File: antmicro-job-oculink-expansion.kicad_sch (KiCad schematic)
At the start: 105 parts, among them J1 OCuLink_x4_Amphenol_G14A42121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, J2 Plug_Samtec_ERM8_2x40_ERM8-04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, U1 MAX3373EEKA+, U2 PI3EQX16904GL, U3 PI3EQX16904GL

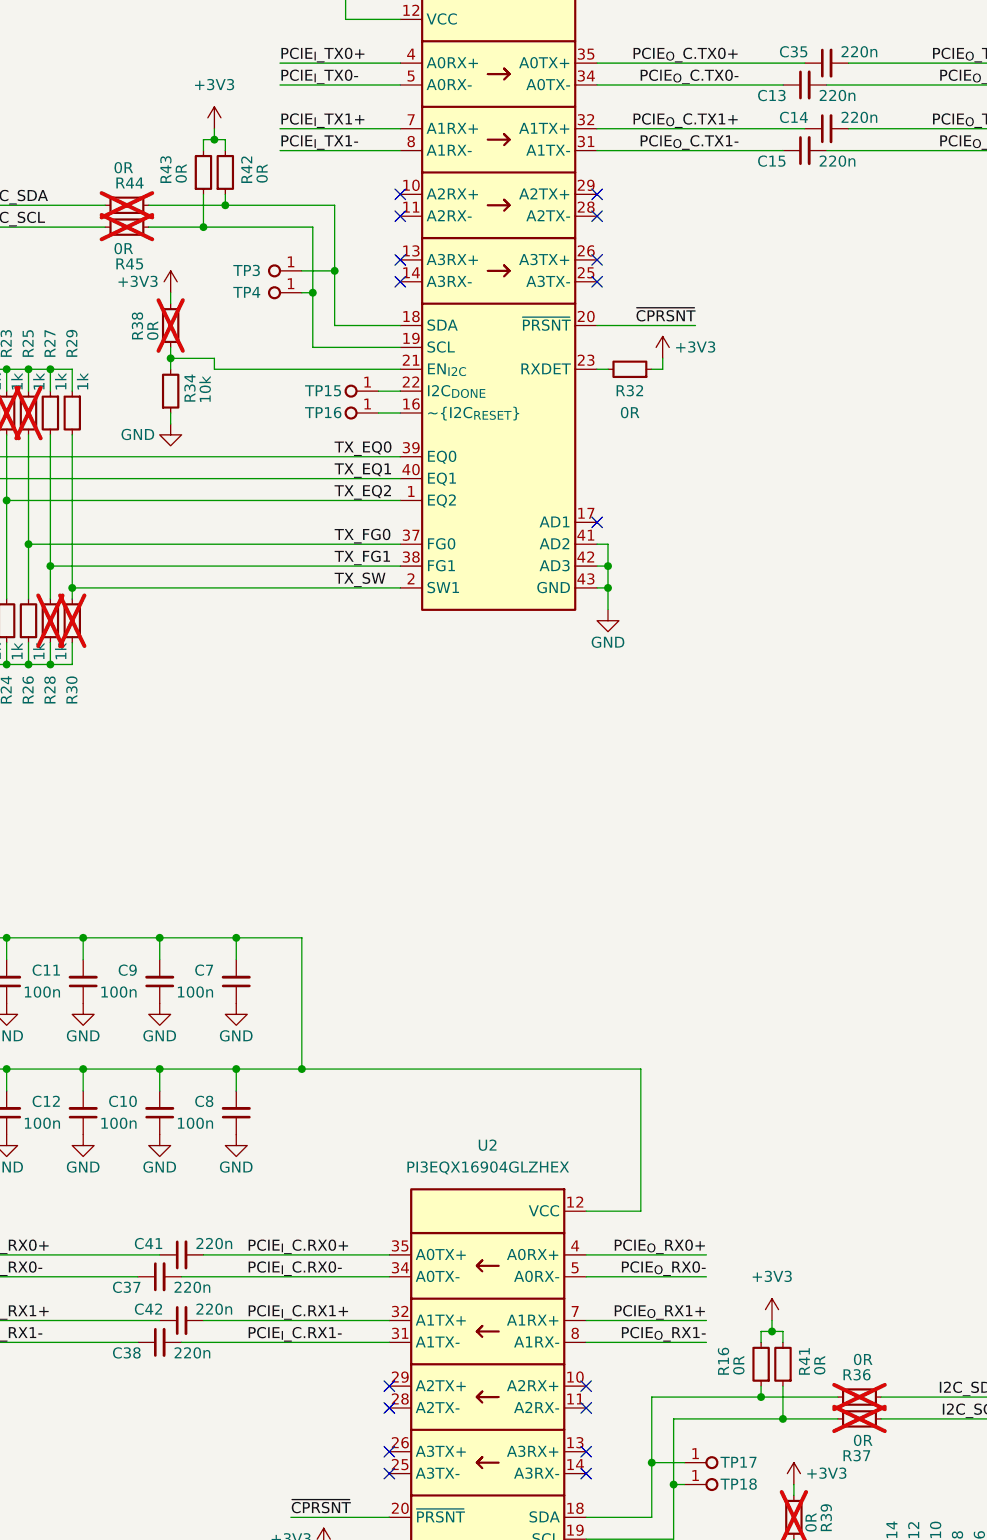
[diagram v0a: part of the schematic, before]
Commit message: [#76297] Fix I2C pull-up resistor value
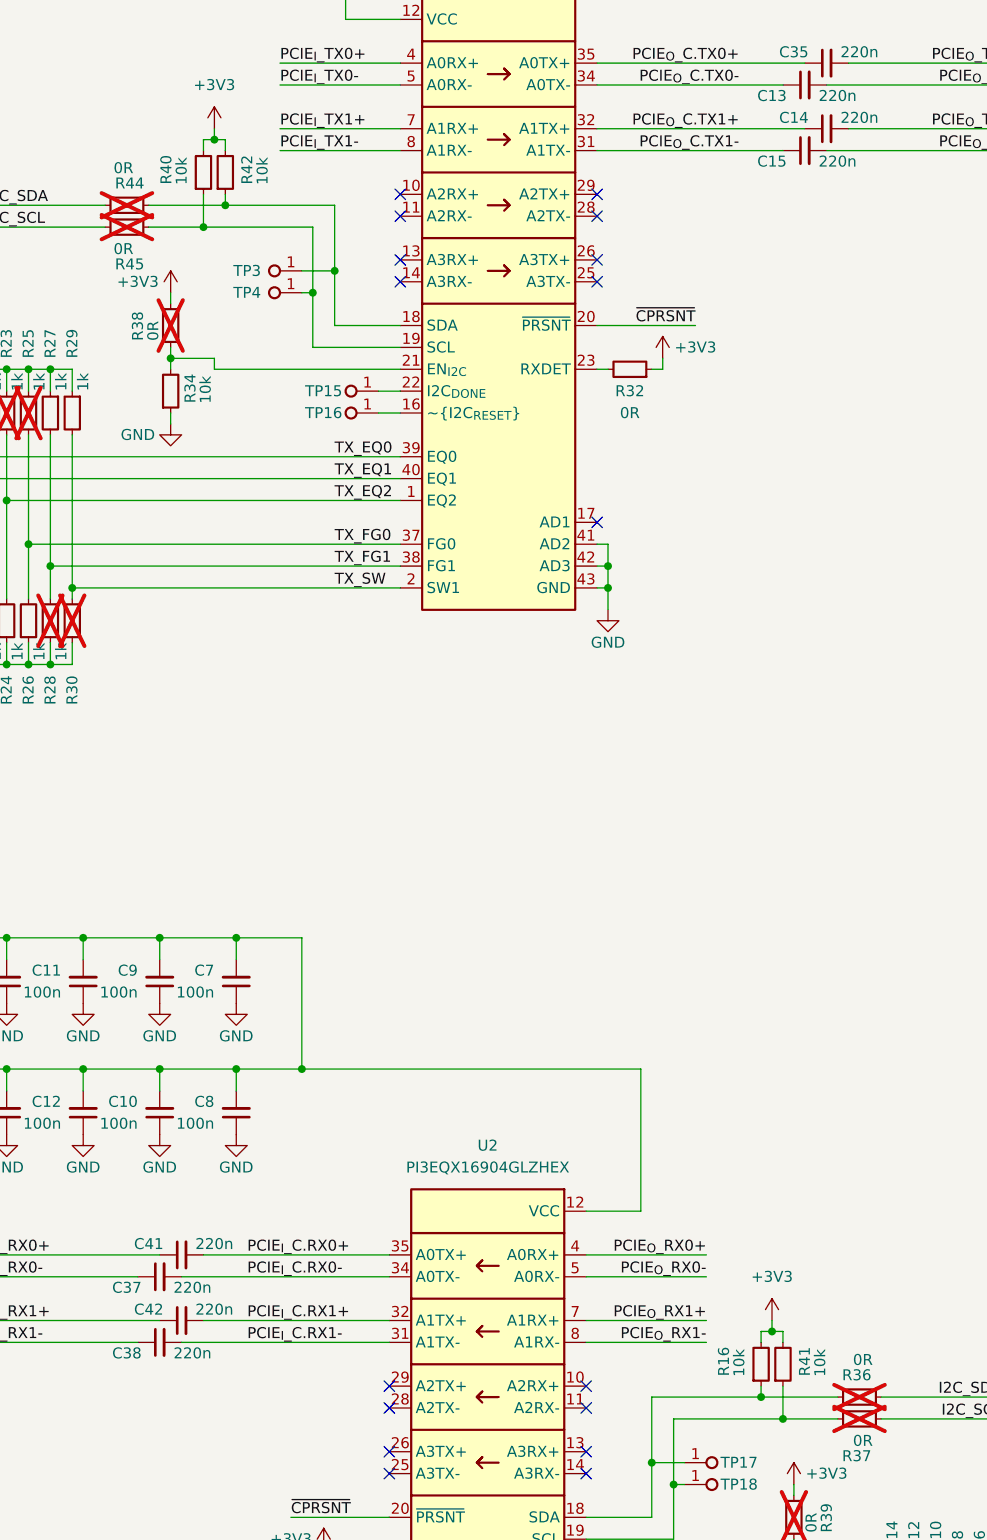
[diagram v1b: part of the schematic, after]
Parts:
- removed R16, R41, R42, R43: R_0R_0402, antmicro-footprints:R_0402_1005Metric, symbol antmicroResistors0402:R_0R_0402
- added R16, R40, R41, R42: R_10k_0402, antmicro-footprints:R_0402_1005Metric, symbol antmicroResistors0402:R_10k_0402
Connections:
- net +3V3: now also R16.2, R40.2, R41.2, R42.2
- net at R36.2, TP17.1, U2.18 (SDA): now also R16.1
- net at R44.2, TP3.1, U3.18 (SDA): now also R42.1
- net at R45.2, TP4.1, U3.19 (SCL): now also R40.1
- net at R37.2, TP18.1, U2.19 (SCL): now also R41.1

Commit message: [#76297] Fix Antmicro logo footprint not matching schematic
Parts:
- N2, N4: footprint antmicro-footprints:antmicro-logo -> antmicro-footprints:antmicro-logo_scaled_15mm
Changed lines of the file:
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@@
 			)
 		)
-		(property "Footprint" "antmicro-footprints:antmicro-logo"
+		(property "Footprint" "antmicro-footprints:antmicro-logo_scaled_15mm"
 			(at 60.96 273.05 0)
 			(effects
@@
 			)
 		)
-		(property "Footprint" "antmicro-footprints:antmicro-logo"
+		(property "Footprint" "antmicro-footprints:antmicro-logo_scaled_15mm"
 			(at 60.96 280.67 0)
 			(effects

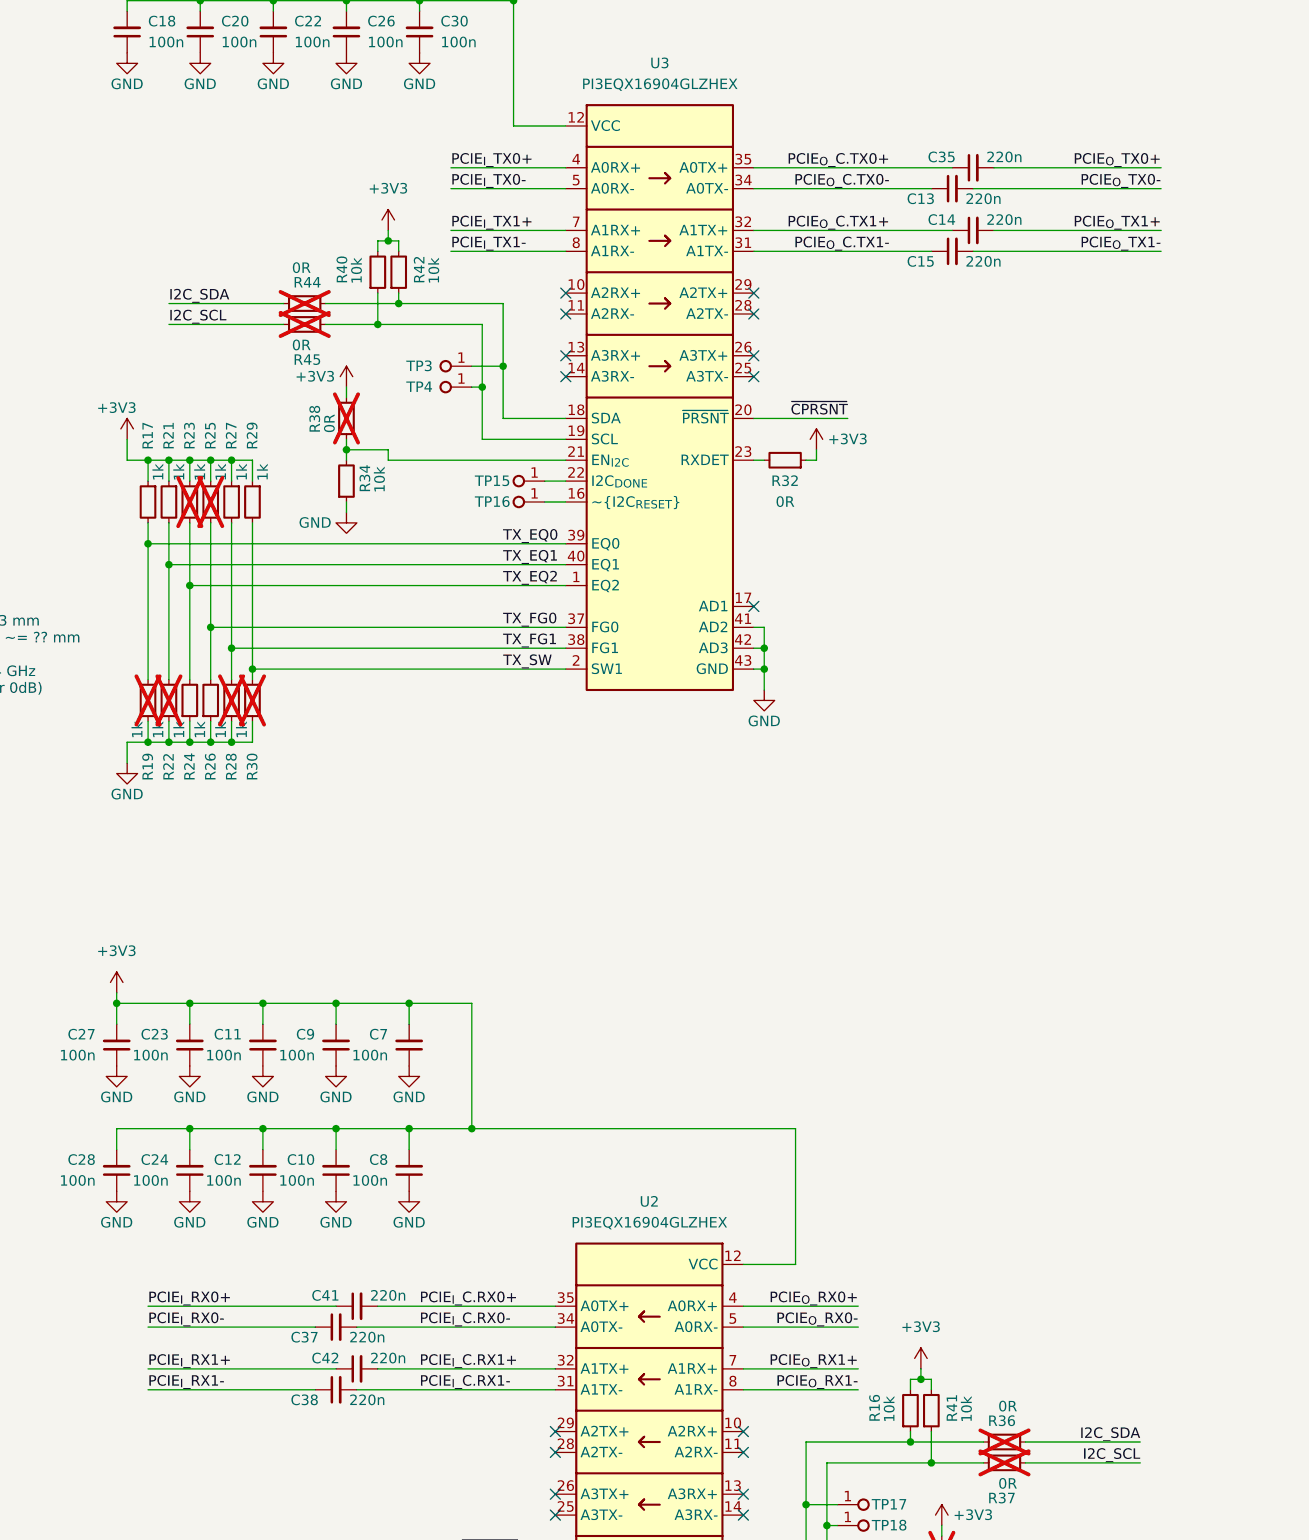
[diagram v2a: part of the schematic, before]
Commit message: [#76297] Reorder redriver PCIe lanes
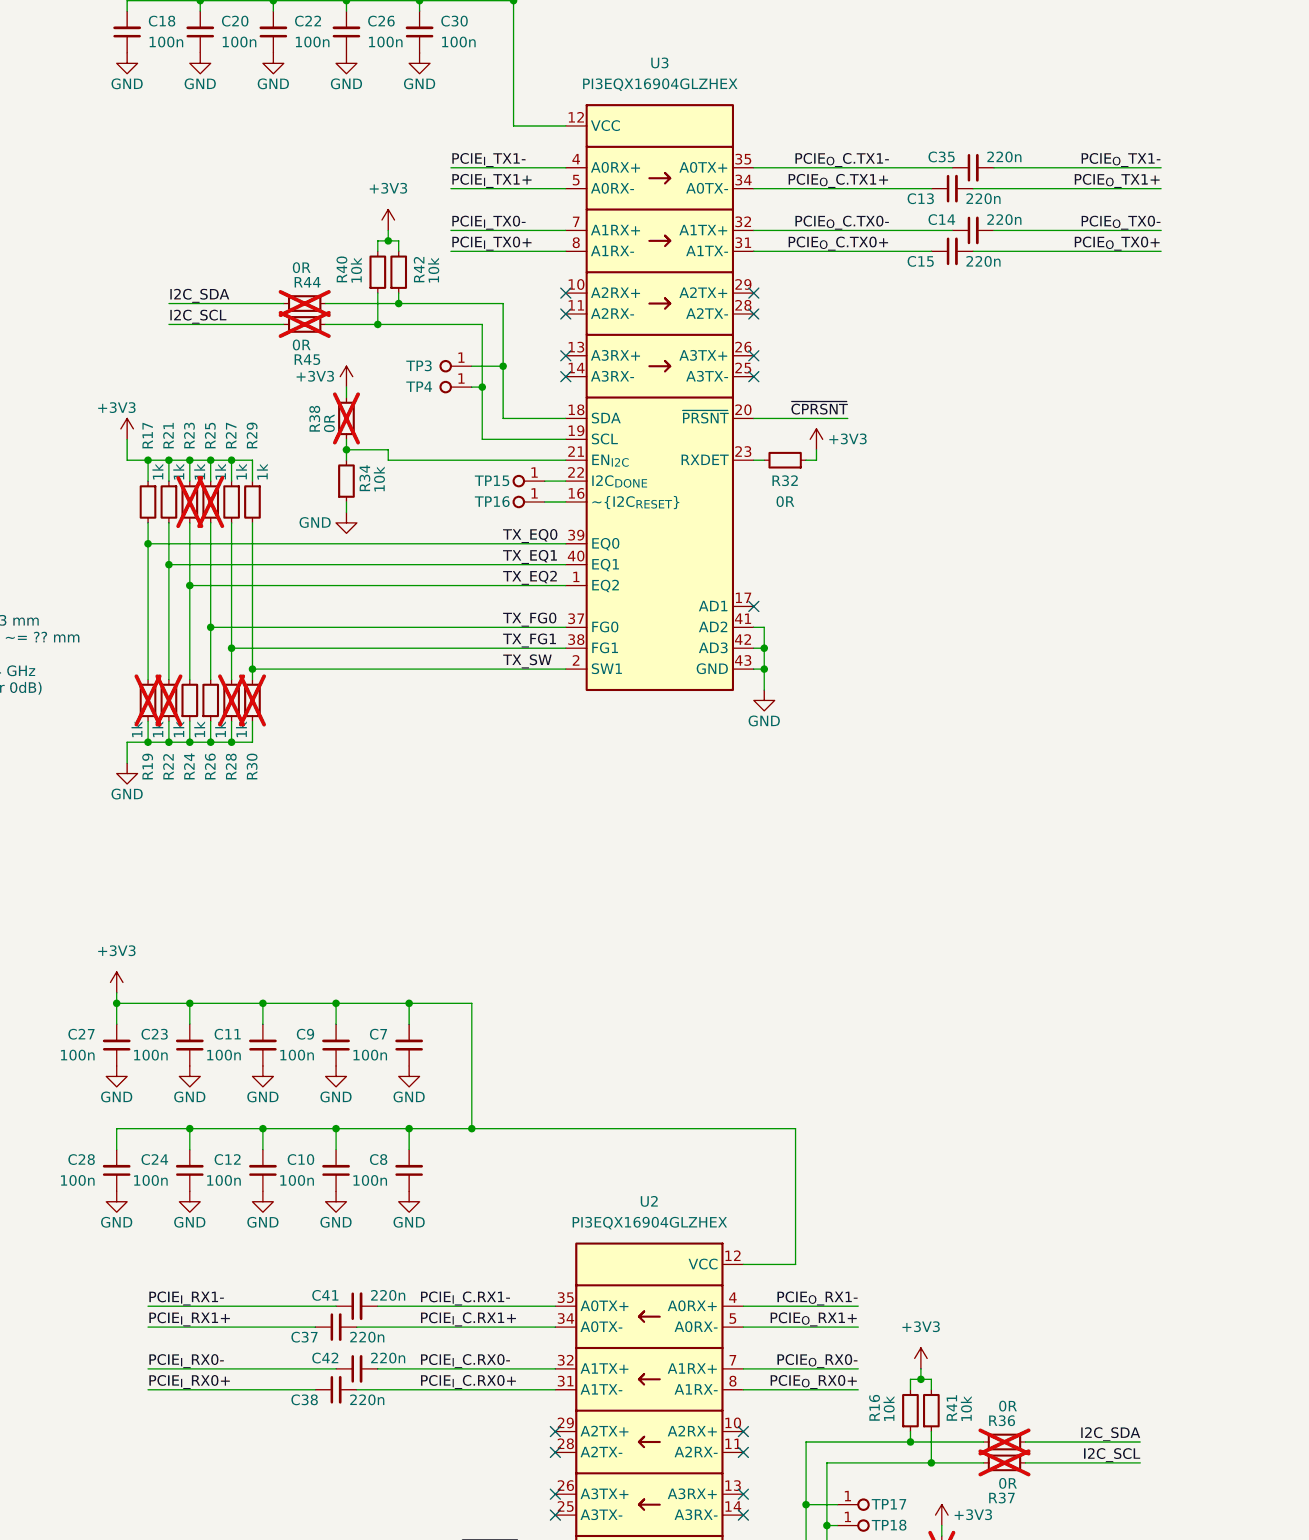
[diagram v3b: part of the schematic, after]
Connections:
- net PCIE_{I}_C.RX0+: now also C38.2, U2.31 (A1TX-); no longer C41.2, U2.35 (A0TX+)
- net PCIE_{I}_C.RX0-: now also C42.2, U2.32 (A1TX+); no longer C37.2, U2.34 (A0TX-)
- net PCIE_{I}_C.RX1+: now also C37.2, U2.34 (A0TX-); no longer C42.2, U2.32 (A1TX+)
- net PCIE_{I}_C.RX1-: now also C41.2, U2.35 (A0TX+); no longer C38.2, U2.31 (A1TX-)
- net PCIE_{I}_RX0+: now also C38.1; no longer C41.1
- net PCIE_{I}_RX0-: now also C42.1; no longer C37.1
- net PCIE_{I}_RX1+: now also C37.1; no longer C42.1
- net PCIE_{I}_RX1-: now also C41.1; no longer C38.1
- net PCIE_{I}_TX0+: now also U3.8 (A1RX-); no longer U3.4 (A0RX+)
- net PCIE_{I}_TX0-: now also U3.7 (A1RX+); no longer U3.5 (A0RX-)
- net PCIE_{I}_TX1+: now also U3.5 (A0RX-); no longer U3.7 (A1RX+)
- net PCIE_{I}_TX1-: now also U3.4 (A0RX+); no longer U3.8 (A1RX-)
- net PCIE_{O}_C.TX0+: now also C15.1, U3.31 (A1TX-); no longer C35.1, U3.35 (A0TX+)
- net PCIE_{O}_C.TX0-: now also C14.1, U3.32 (A1TX+); no longer C13.1, U3.34 (A0TX-)
- net PCIE_{O}_C.TX1+: now also C13.1, U3.34 (A0TX-); no longer C14.1, U3.32 (A1TX+)
- net PCIE_{O}_C.TX1-: now also C35.1, U3.35 (A0TX+); no longer C15.1, U3.31 (A1TX-)
- net PCIE_{O}_RX0+: now also U2.8 (A1RX-); no longer U2.4 (A0RX+)
- net PCIE_{O}_RX0-: now also U2.7 (A1RX+); no longer U2.5 (A0RX-)
- net PCIE_{O}_RX1+: now also U2.5 (A0RX-); no longer U2.7 (A1RX+)
- net PCIE_{O}_RX1-: now also U2.4 (A0RX+); no longer U2.8 (A1RX-)
- net PCIE_{O}_TX0+: now also C15.2; no longer C35.2
- net PCIE_{O}_TX0-: now also C14.2; no longer C13.2
- net PCIE_{O}_TX1+: now also C13.2; no longer C14.2
- net PCIE_{O}_TX1-: now also C35.2; no longer C15.2
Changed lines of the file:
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@@
 	)
 	(label "PCIE_{O}_TX1-"
-		(at 273.05 73.66 180)
+		(at 273.05 63.5 180)
 		(fields_autoplaced yes)
 		(effects
@@
 	)
 	(label "PCIE_{I}_TX0+"
-		(at 186.69 63.5 0)
+		(at 186.69 73.66 0)
 		(fields_autoplaced yes)
 		(effects
@@
 	)
 	(label "PCIE_{O}_RX0+"
-		(at 236.22 201.93 180)
+		(at 236.22 212.09 180)
 		(fields_autoplaced yes)
 		(effects
@@
 	)
 	(label "PCIE_{I}_RX0+"
-		(at 149.86 201.93 0)
+		(at 149.86 212.09 0)
 		(fields_autoplaced yes)
 		(effects
@@
 	)
 	(label "PCIE_{I}_TX1-"
-		(at 186.69 73.66 0)
+		(at 186.69 63.5 0)
 		(fields_autoplaced yes)
 		(effects
@@
 	)
 	(label "PCIE_{I}_RX0-"
-		(at 149.86 204.47 0)
+		(at 149.86 209.55 0)
 		(fields_autoplaced yes)
 		(effects
@@
 	)
 	(label "PCIE_{I}_RX1+"
-		(at 149.86 209.55 0)
+		(at 149.86 204.47 0)
 		(fields_autoplaced yes)
 		(effects
@@
 	)
 	(label "PCIE_{I}_C.RX1+"
-		(at 182.88 209.55 0)
+		(at 182.88 204.47 0)
 		(fields_autoplaced yes)
 		(effects
@@
 	)
 	(label "PCIE_{O}_C.TX0+"
-		(at 240.03 63.5 180)
+		(at 240.03 73.66 180)
 		(fields_autoplaced yes)
 		(effects
@@
 	)
 	(label "PCIE_{O}_TX0+"
-		(at 273.05 63.5 180)
+		(at 273.05 73.66 180)
 		(fields_autoplaced yes)
 		(effects
@@
 	)
 	(label "PCIE_{I}_RX1-"
-		(at 149.86 212.09 0)
+		(at 149.86 201.93 0)
 		(fields_autoplaced yes)
 		(effects
@@
 	)
 	(label "PCIE_{O}_RX1-"
-		(at 236.22 212.09 180)
+		(at 236.22 201.93 180)
 		(fields_autoplaced yes)
 		(effects
@@
 	)
 	(label "PCIE_{O}_C.TX0-"
-		(at 240.03 66.04 180)
+		(at 240.03 71.12 180)
 		(fields_autoplaced yes)
 		(effects
@@
 	)
 	(label "PCIE_{I}_C.RX0+"
-		(at 182.88 201.93 0)
+		(at 182.88 212.09 0)
 		(fields_autoplaced yes)
 		(effects
@@
 	)
 	(label "PCIE_{O}_RX1+"
-		(at 236.22 209.55 180)
+		(at 236.22 204.47 180)
 		(fields_autoplaced yes)
 		(effects
@@
 	)
 	(label "PCIE_{I}_TX0-"
-		(at 186.69 66.04 0)
+		(at 186.69 71.12 0)
 		(fields_autoplaced yes)
 		(effects
@@
 	)
 	(label "PCIE_{O}_C.TX1-"
-		(at 240.03 73.66 180)
+		(at 240.03 63.5 180)
 		(fields_autoplaced yes)
 		(effects
@@
 	)
 	(label "PCIE_{O}_TX1+"
-		(at 273.05 71.12 180)
+		(at 273.05 66.04 180)
 		(fields_autoplaced yes)
 		(effects
@@
 	)
 	(label "PCIE_{O}_RX0-"
-		(at 236.22 204.47 180)
+		(at 236.22 209.55 180)
 		(fields_autoplaced yes)
 		(effects
@@
 	)
 	(label "PCIE_{O}_C.TX1+"
-		(at 240.03 71.12 180)
+		(at 240.03 66.04 180)
 		(fields_autoplaced yes)
 		(effects
@@
 	)
 	(label "PCIE_{O}_TX0-"
-		(at 273.05 66.04 180)
+		(at 273.05 71.12 180)
 		(fields_autoplaced yes)
 		(effects
@@
 	)
 	(label "PCIE_{I}_C.RX0-"
-		(at 182.88 204.47 0)
+		(at 182.88 209.55 0)
 		(fields_autoplaced yes)
 		(effects
@@
 	)
 	(label "PCIE_{I}_C.RX1-"
-		(at 182.88 212.09 0)
+		(at 182.88 201.93 0)
 		(fields_autoplaced yes)
 		(effects
@@
 	)
 	(label "PCIE_{I}_TX1+"
-		(at 186.69 71.12 0)
-		(fields_autoplaced yes)
-		(effects
+		(at 186.69 66.04 0)
+		(fields_autoplaced yes)
+		(effects
